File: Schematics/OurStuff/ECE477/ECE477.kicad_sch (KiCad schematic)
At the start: 65 parts, among them J1 USB_B_Micro, J2 Barrel_Jack, J3 OLED JST PH 7pin, J7 D30V30F3, Q1 SS8050-G, Q2 SS8050-G, U1 ESP32-WROOM-32E, U2 CP2102N-Axx-xQFN28

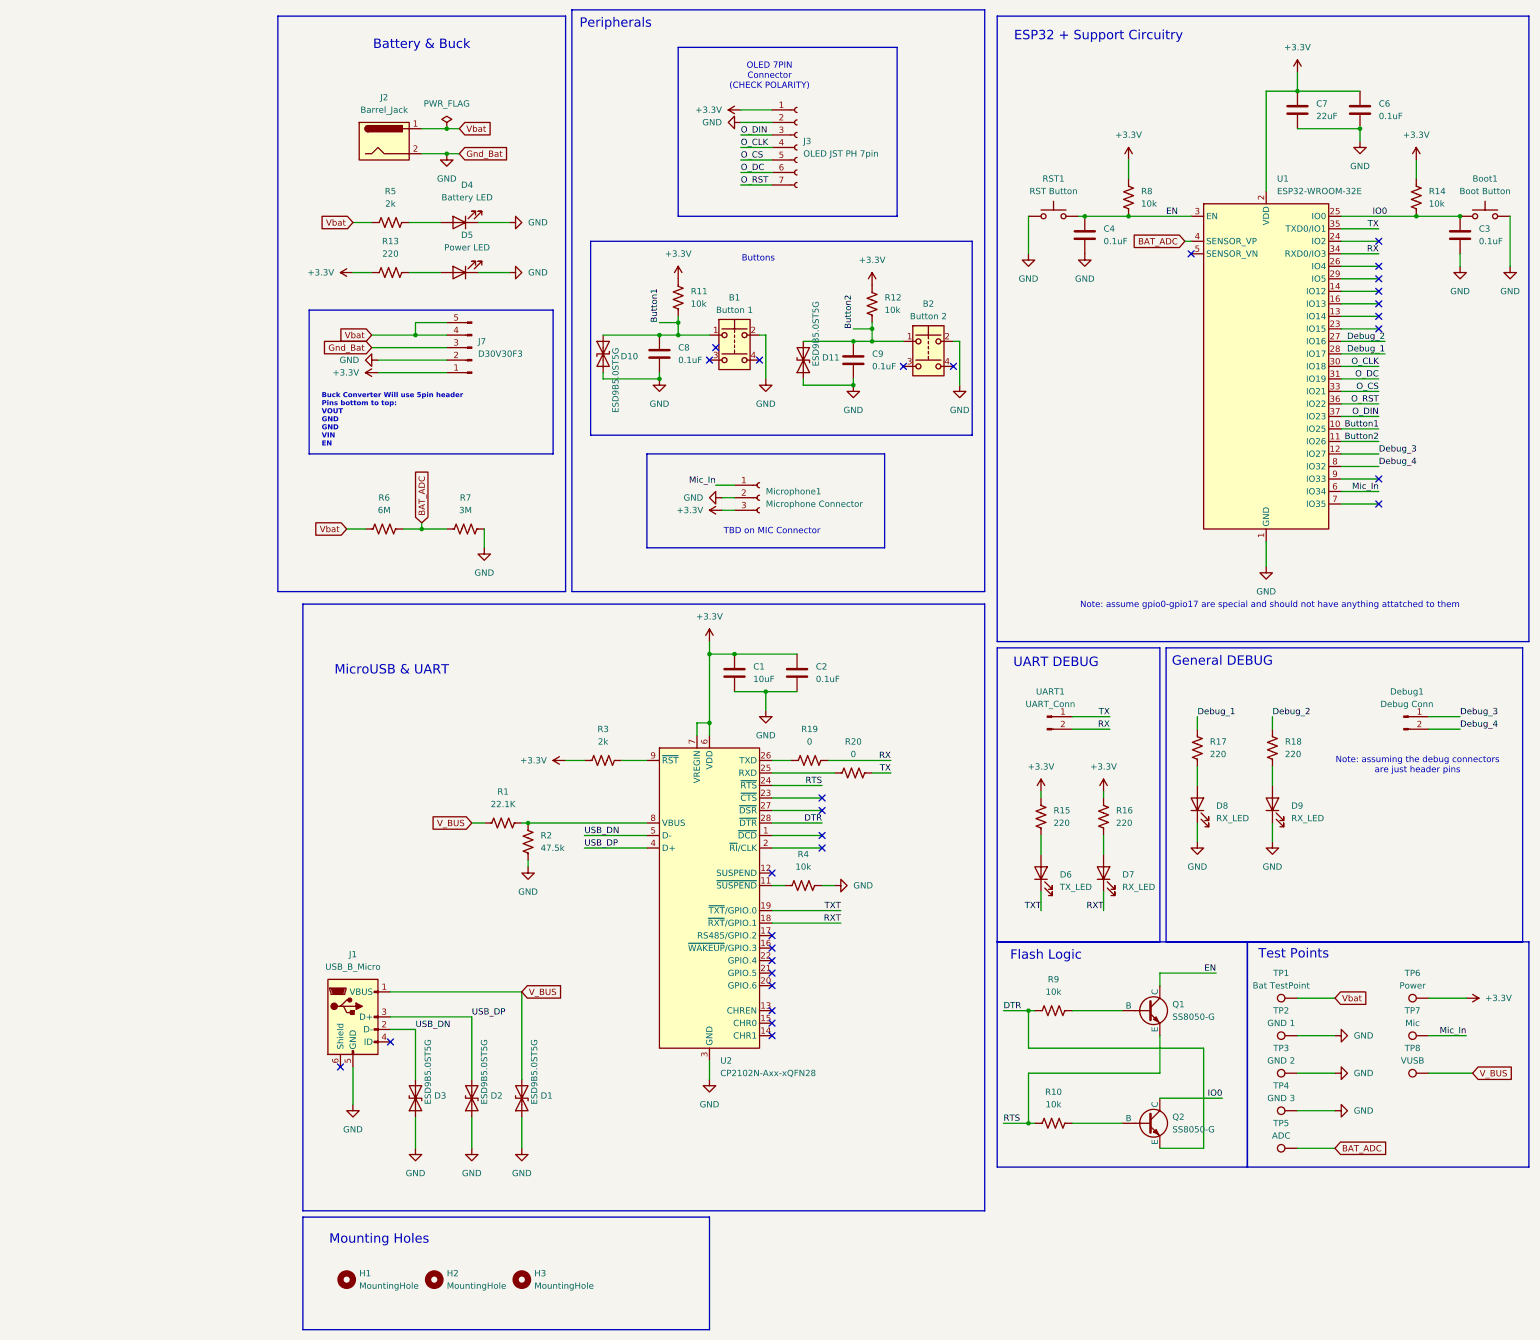
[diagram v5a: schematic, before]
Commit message: swapped ESD protection on schematic
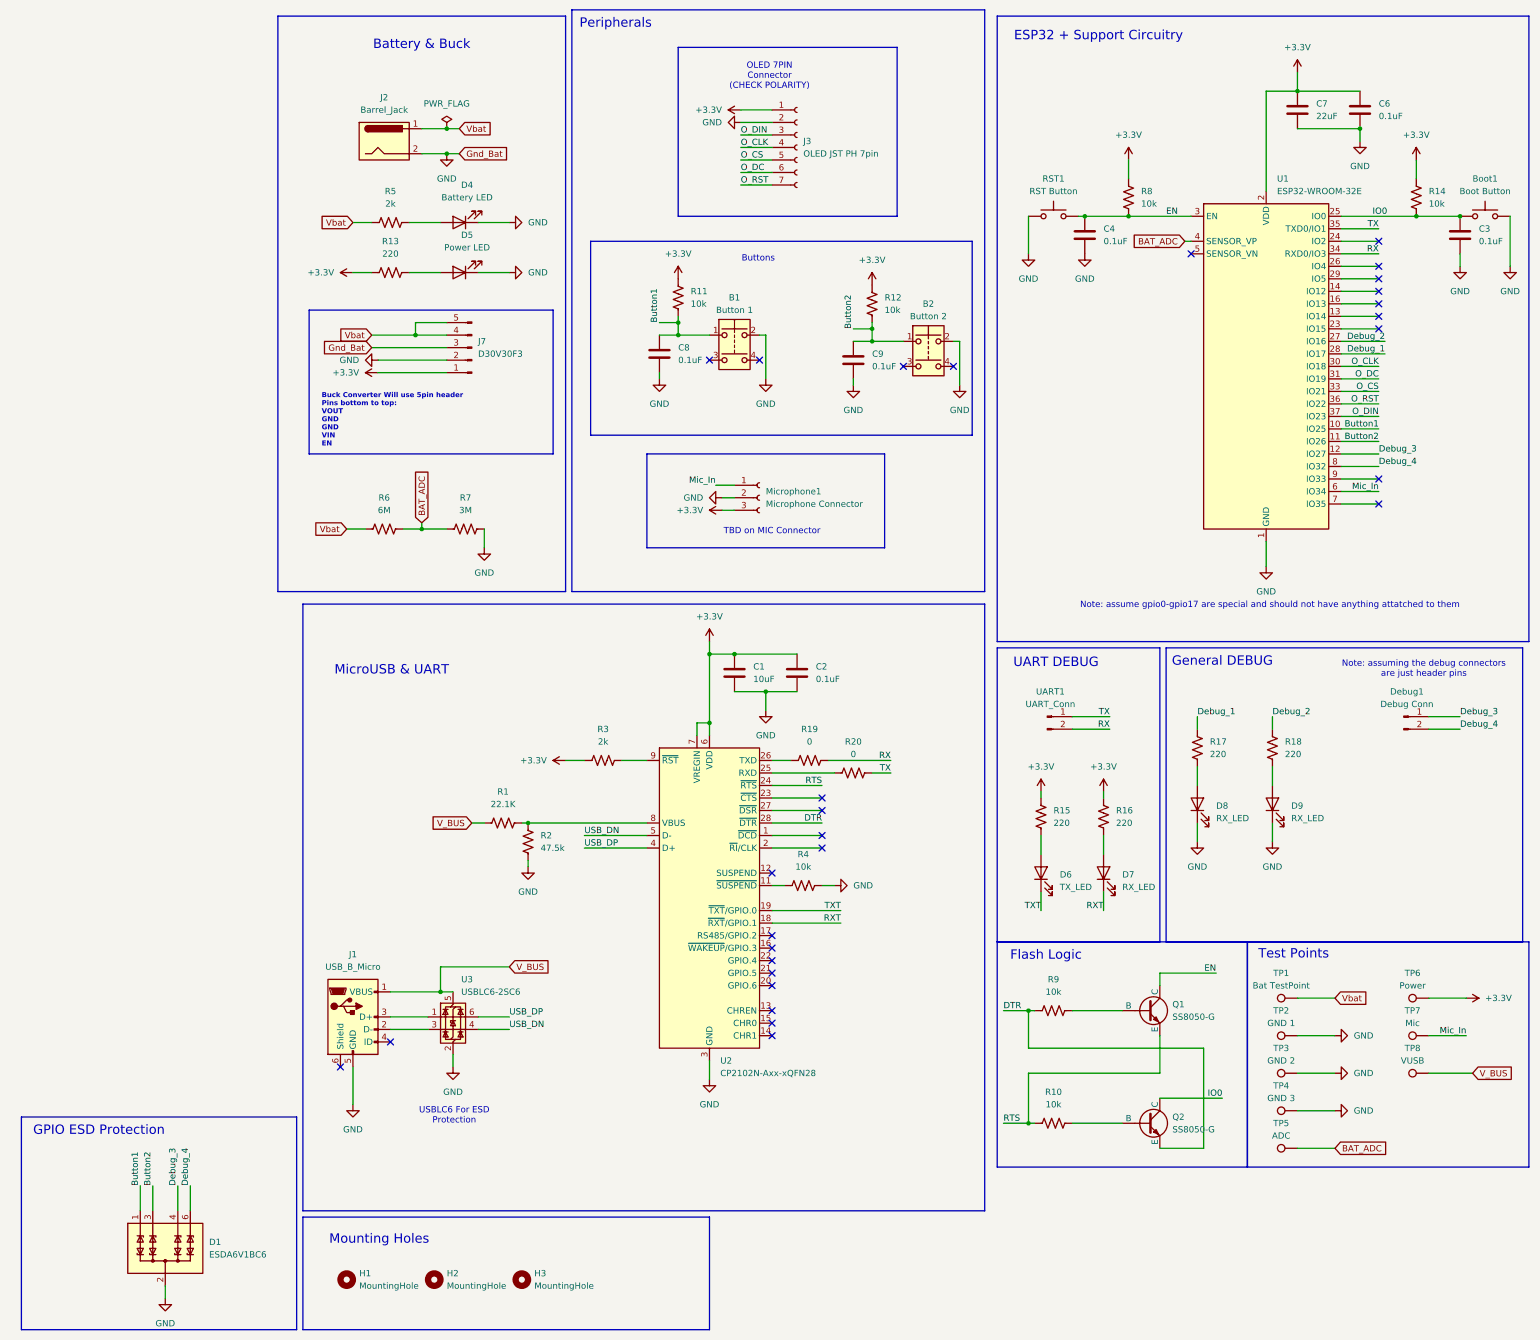
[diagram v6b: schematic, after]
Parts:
- removed D1, D10, D11, D2, D3: ESD9B5.0ST5G, Diode_SMD:D_SOD-923, symbol Device:D_TVS
- added D1: ESDA6V1BC6, Package_TO_SOT_SMD:SOT-23-6, symbol Power_Protection:ESDA6V1BC6
- added U3: USBLC6-2SC6, Package_TO_SOT_SMD:SOT-23-6, symbol Power_Protection:USBLC6-2SC6
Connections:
- net Button1: now also D1.1 (TVS1)
- net Button2: now also D1.3 (TVS2)
- net Debug_3: now also D1.4 (TVS3)
- net Debug_4: now also D1.6 (TVS4)
- net GND: now also D1.2 (COM), D1.5 (COM), U3.2 (GND)
- net USB_DN: now also U3.4 (I/O2); no longer J1.2 (D-)
- net USB_DP: now also U3.6 (I/O1); no longer J1.3 (D+)
- net V_BUS: now also U3.5 (VBUS)
- new net: J1.2 (D-), U3.3 (I/O2)
- new net: J1.3 (D+), U3.1 (I/O1)
- no-connect marks 30 -> 29
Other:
- note added: "GPIO ESD Protection"
- note added: "USBLC6 For ESD Protection"

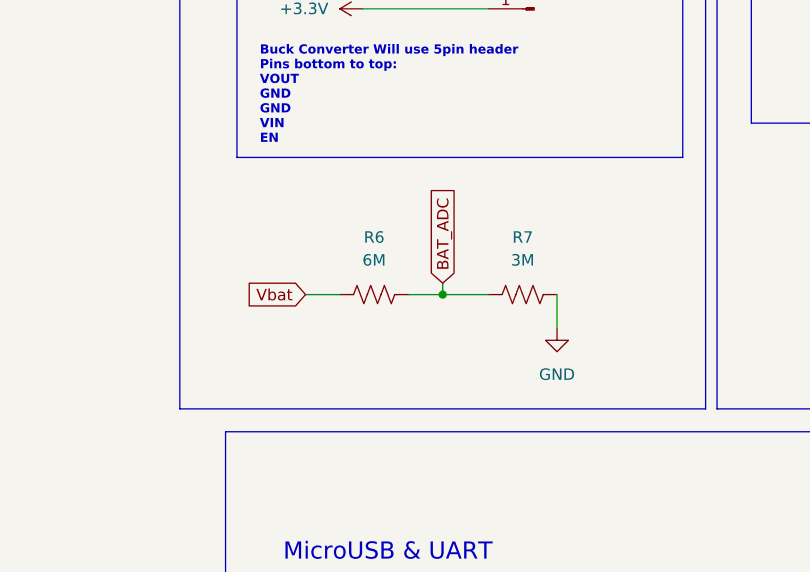
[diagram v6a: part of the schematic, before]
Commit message: added bat mon capacitor
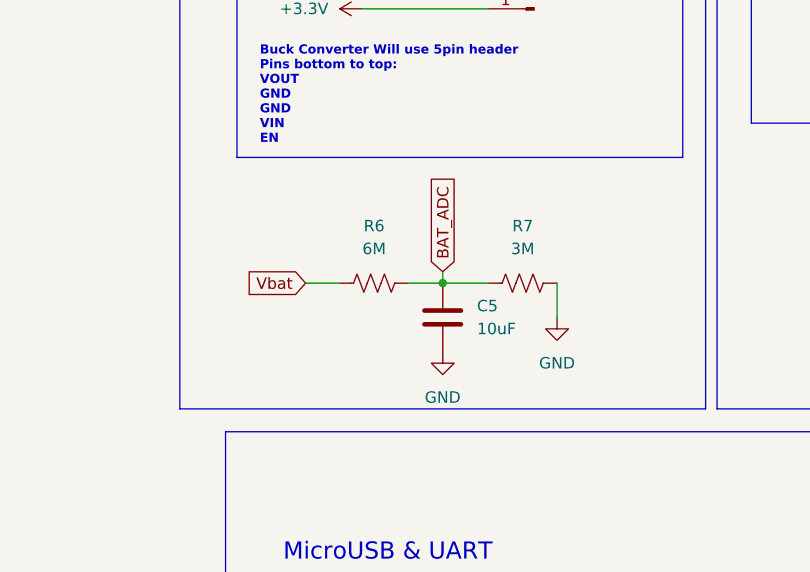
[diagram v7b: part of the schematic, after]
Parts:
- added C5: 10uF, Capacitor_SMD:C_0805_2012Metric_Pad1.18x1.45mm_HandSolder, symbol Device:C
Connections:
- net BAT_ADC: now also C5.1
- net GND: now also C5.2
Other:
- moved on the sheet: R6, R7

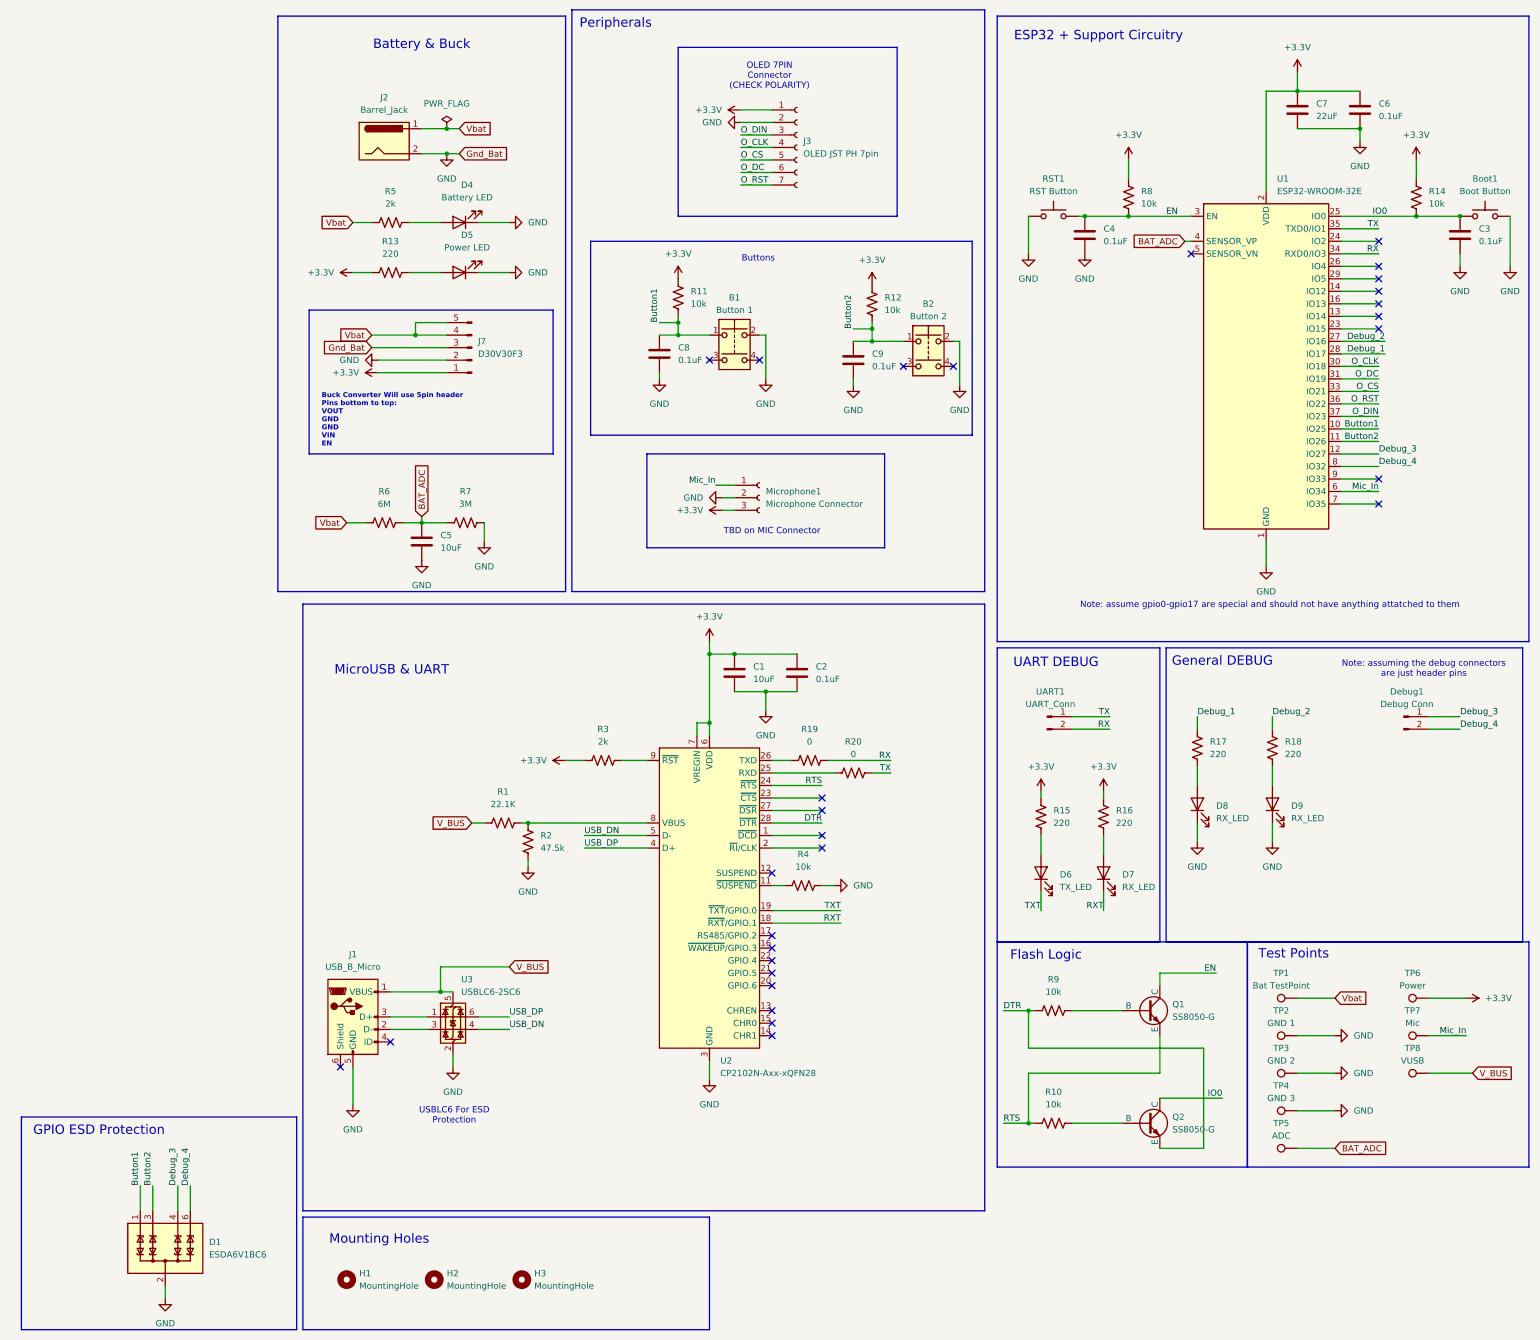
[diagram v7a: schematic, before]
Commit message: added ferrite bead and fixed mic
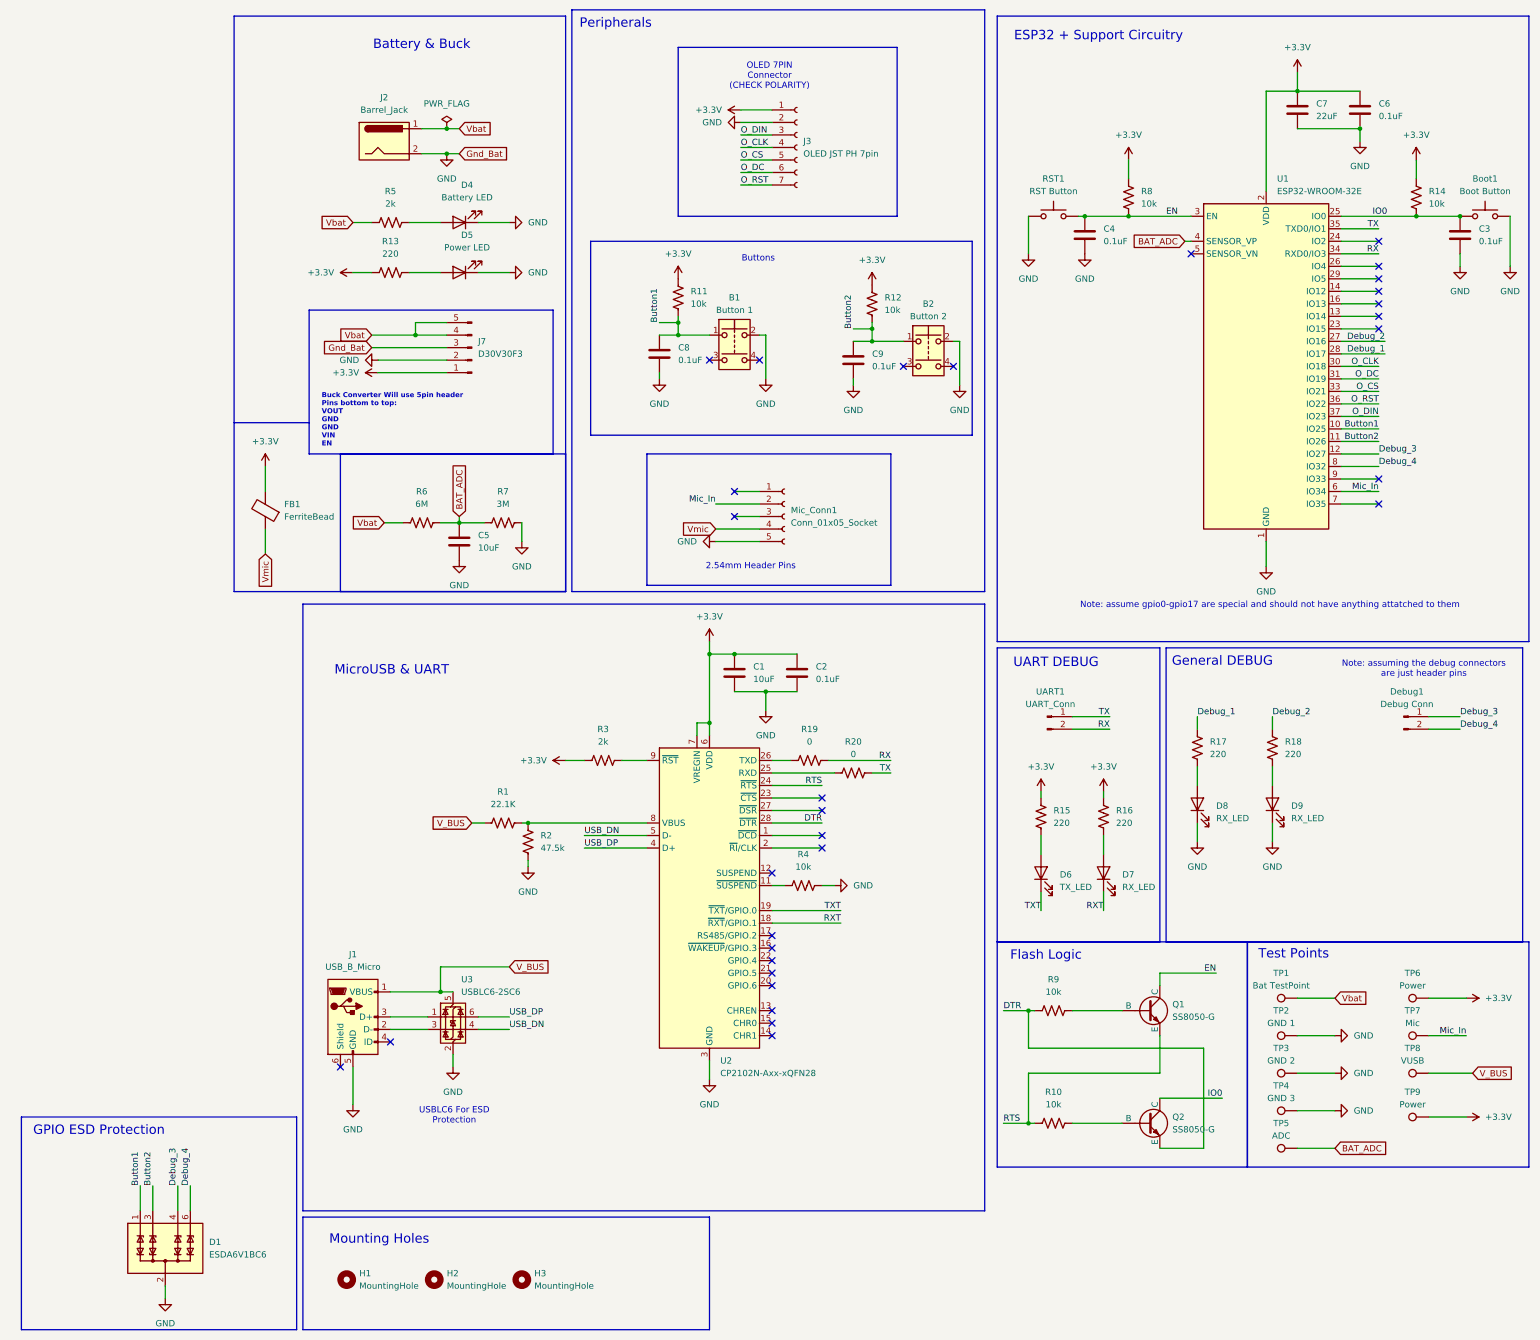
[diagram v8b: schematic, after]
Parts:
- removed Microphone1: Microphone Connector, Connector_PinHeader_2.54mm:PinHeader_1x03_P2.54mm_Vertical, symbol Connector:Conn_01x03_Socket
- added FB1: FerriteBead, Inductor_SMD:L_0805_2012Metric_Pad1.05x1.20mm_HandSolder, symbol Device:FerriteBead
- added Mic_Conn1: Conn_01x05_Socket, Connector_PinHeader_2.54mm:PinHeader_1x05_P2.54mm_Vertical, symbol Connector:Conn_01x05_Socket
- added TP9: Power, TestPoint:TestPoint_Keystone_5010-5014_Multipurpose, symbol Connector:TestPoint
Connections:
- net +3.3V: now also FB1.2, TP9.1
- net GND: now also Mic_Conn1.5 (Pin_5)
- net Mic_In: now also Mic_Conn1.2 (Pin_2)
- new net Vmic: FB1.1, Mic_Conn1.4 (Pin_4)
- no-connect marks 29 -> 31
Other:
- note added: "2.54mm Header Pins"
- note removed: "TBD on MIC Connector"
- moved on the sheet: C5, R6, R7
